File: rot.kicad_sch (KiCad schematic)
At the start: 35 parts, among them J3 52991-0508, J4 M20-7830642, U2 W25Q32JVSSIQ_TR, U3 W25Q32JVSSIQ_TR, U4 W25Q32JVSSIQ_TR, U5 W25Q32JVSSIQ_TR

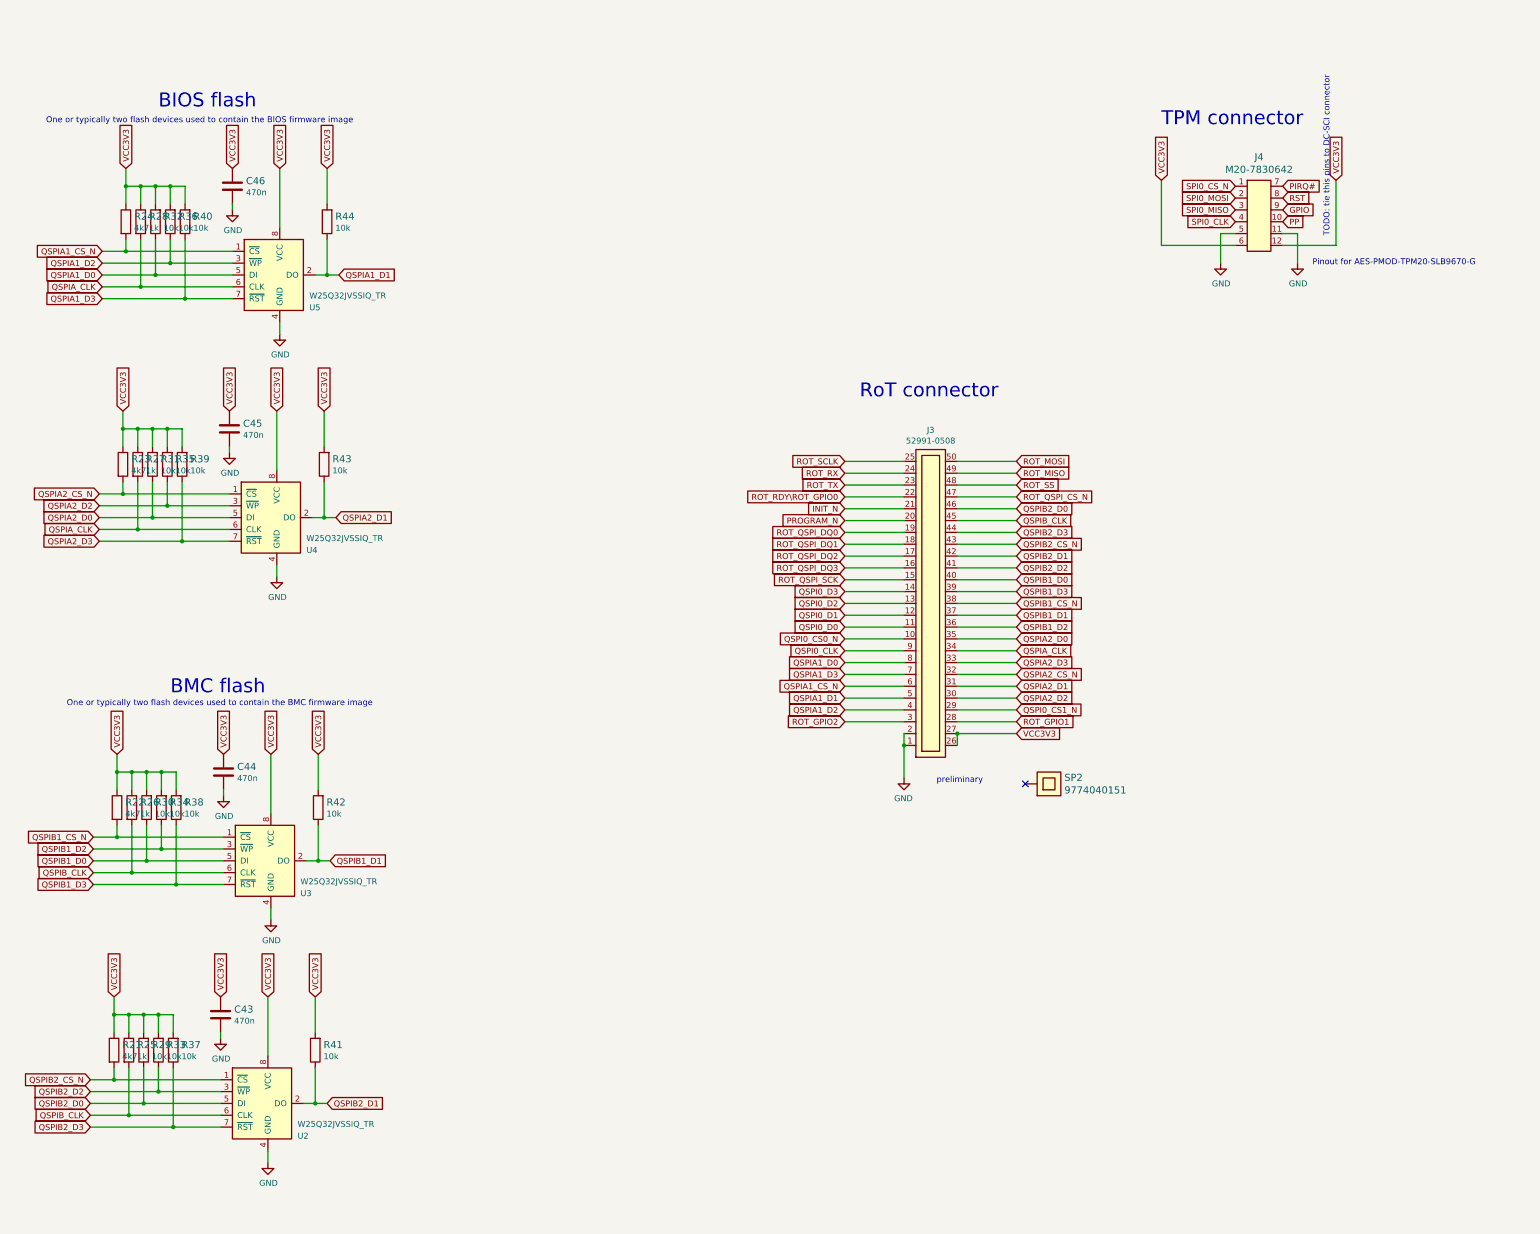
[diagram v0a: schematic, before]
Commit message: [#61392] Convert project to KiCad 7
[#61392] Run globlib

[#61392] Allign components to the grid

[#61392] Update oshw and antmicro logo

[#61392] Standarize ethernet sheet

[#61392] Standarize pcie-conn sheet

[#61392] Standarize rot sheet

[#61392] Standarize edge-connector sheet

[#61392] WIP:Standarize interfaces sheet

[#61392] WIP: Route interfaces sheet

[#61392] Finish standarizing interfaces sheet

[#61392] Update interfaces sheet with fixed 2N7002

[#61392] WIP:Standarize ddr3 sheet

[#61392] Standarize ddr3 sheet

[#61392] Standarize power-supply sheet

[#61392] Standarize fpga power-supply sheet

[#61392] Remove TODO comments from power-banks sheet

[#61392] Standarize fpga-banks sheet

[#61392] Ignore Input pins not driven ERC

[#61392] Clear off grid ERCs

[#61392] Exclude ERC DDR3_VTT_EN NC

[#61392] Bump rev to 1.2.1

[#61392] Bump PCB rev to 1.2.1
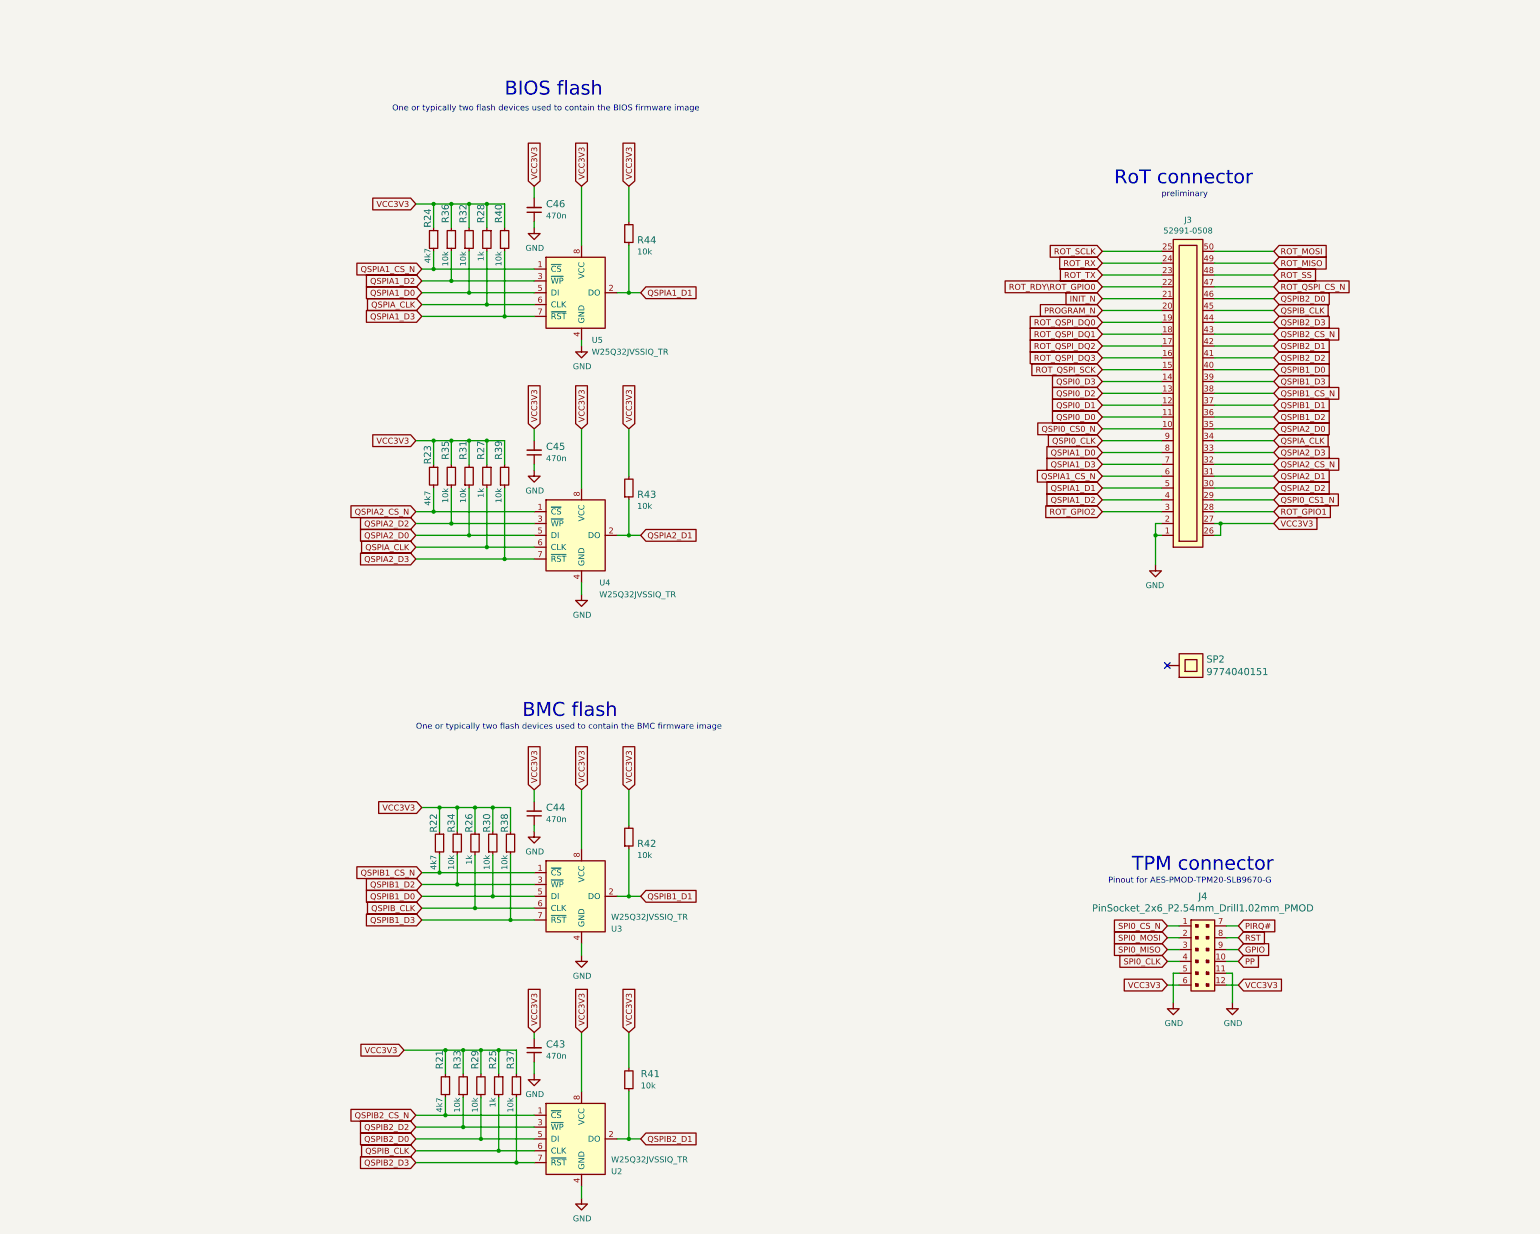
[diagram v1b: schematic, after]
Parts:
- C43, C44, C45, C46: footprint ecp5-dc-scm-footprints:0402-cap -> antmicro-footprints:C_0402_1005Metric; symbol ecp5-dc-scm:C_470n_0402 -> antmicroCapacitors0402:C_470n_0402; Author (none) -> Antmicro; License (none) -> Apache-2.0; Public (none) -> False
- J4: value M20-7830642 -> PinSocket_2x6_P2.54mm_Drill1.02mm_PMOD; footprint ecp5-dc-scm-footprints:PinHeader_6x2_P2.54mm_Vertical_pmod -> antmicro-footprints:PinSocket_2x6_P2.54mm_Drill1.02mm_PMOD; symbol ecp5-dc-scm:M20-7830642 -> antmicroGenericPinSockets:PinSocket_2x6_P2.54mm_Drill1.02mm_PMOD; Author (none) -> Antmicro; License (none) -> Apache-2.0; Manufacturer Molex -> Harwin
- R21, R22, R23, R24: footprint ecp5-dc-scm-footprints:0402-res -> antmicro-footprints:R_0402_1005Metric; symbol ecp5-dc-scm:R_4k7_0402 -> antmicroResistors0402:R_4k7_0402; Author (none) -> Antmicro; License (none) -> Apache-2.0; MPN ERJ2GEJ472X -> CR0402-FX-4701GLF; Manufacturer PANASONIC_ELECTRONIC_COMPONENTS -> Bourns; Public (none) -> False; Tolerance (none) -> 1%
- R25, R26, R27, R28: footprint ecp5-dc-scm-footprints:0402-res -> antmicro-footprints:R_0402_1005Metric; symbol ecp5-dc-scm:R_1k_0402 -> antmicroResistors0402:R_1k_0402; Author (none) -> Antmicro; License (none) -> Apache-2.0; Manufacturer BOURNS -> Bourns; Public (none) -> False; Tolerance (none) -> 1%
- R29, R30, R31, R32, R33, R34, R35, R36, R37, R38, R39, R40, R41, R42, R43, R44: footprint ecp5-dc-scm-footprints:0402-res -> antmicro-footprints:R_0402_1005Metric; symbol ecp5-dc-scm:R_10k_0402 -> antmicroResistors0402:R_10k_0402; Author (none) -> Antmicro; License (none) -> Apache-2.0; MPN CRCW040210K0FKEDHP -> CR0402-FX-1002GLF; Manufacturer VISHAY -> Bourns; Public (none) -> False; Tolerance (none) -> 1%
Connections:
- net GND: now also C43.1, C44.1, C45.1, C46.1; no longer C43.2, C44.2, C45.2, C46.2
- net VCC3V3: now also C43.2, C44.2, C45.2, C46.2; no longer C43.1, C44.1, C45.1, C46.1
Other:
- note removed: "TODO: tie this pins to DC-SCI connector"
- moved on the sheet: C43, C44, C45, C46, J3, R21, R22, R23, R24, R25, R26, R27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

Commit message: [#61392] Import changes to the PCB
[#61392] Fix D2 orientation

[#61392] Fix J2 J1 D6 orientation

[#61392] WIP: PCB Fix caps orienations

[#61392] PCB Fix caps orienations

[#61392] Fix missalligned edge cuts

[#61392] Sync Sch with PCB

[#61392] Fix silk clipped by edge cuts

[#61392] Ignore TP no courtyard drc

[#61392] Update C_0603 footprints

[#61392] Update R_0402 footprints

[#61392] Update Sot-23 footprints

[#61392] Update QFN and IHLP footprints

[#61392] Update remaining footprints

[#61392] Change minimal text height to 0.7mm

[#61392] Clear remaining Silk DRCs

[#61392] Update TPS51200DRCT symbol

[#61392] Update 9774040151

[#61392] Update W25Q32JVS

[#61392] Update ECS-3225MVQ-1000CN-TR

[#61392] Clean ERC

[#61392] Remove obsolete files

[#61392] Synhronize components with library

[#61392] Remove globlib leftovers

[#61392] Synchronize components with libraries (WiP)

[#61392] Clean ERC and DRC

[#61392] Set J5 to DNP

[#61392] Add PCB SHA string, update layer names

[#61392] Update assets

[#62567] Add stackup.csv

[#62567] Input elecric constants for the board stackup

[#62567] Update stackup.csv
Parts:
- removed J3: 52991-0508, ecp5-dc-scm-footprints:529910508, symbol ecp5-dc-scm:52991-0508
- removed SP2: 9774040151, ecp5-dc-scm-footprints:9774040151, symbol ecp5-dc-scm:9774040151
- removed U2, U3, U4, U5: W25Q32JVSSIQ_TR, ecp5-dc-scm-footprints:W25Q32JVSSIQ, symbol ecp5-dc-scm:W25Q32JVSSIQ_TR
- added H2: Spacer_Drill3.7mm_H4mm_9774040151R, antmicro-footprints:Spacer_Drill3.7mm_H4mm_9774040151R, symbol antmicroMechanicalParts:Spacer_Drill3.7mm_H4mm_9774040151R
- added J3: Plug_Molex_SlimStack_2x25_529910508, antmicro-footprints:Conn_Plug_Molex_SlimStack_2x25_529910508, symbol antmicroB2BConnectors:Plug_Molex_SlimStack_2x25_529910508
- added U2, U3, U4, U5: W25Q32JVSSIQ, antmicro-footprints:SOIC-8_5.3x5.3x2mm_P1.27mm, symbol antmicroMemory:W25Q32JVSSIQ
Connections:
- net GND: now also J3.2, J3.4, U2.4 (VSS), U3.4 (VSS), U4.4 (VSS), U5.4 (VSS)
- net INIT_N: now also J3.42
- net PROGRAM_N: now also J3.40
- net QSPI0_CLK: now also J3.18
- net QSPI0_CS0_N: now also J3.20
- net QSPI0_CS1_N: now also J3.7
- net QSPI0_D0: now also J3.22
- net QSPI0_D1: now also J3.24
- net QSPI0_D2: now also J3.26
- net QSPI0_D3: now also J3.28
- net QSPIA1_CS_N: now also J3.12, U5.1 (~{CS})
- net QSPIA1_D0: now also J3.16, U5.5 (SI/IO0)
- net QSPIA1_D1: now also J3.10, U5.2 (SO/IO1)
- net QSPIA1_D2: now also J3.8, U5.3 (~{WP}/IO2)
- net QSPIA1_D3: now also J3.14, U5.7 (~{HOLD}/IO3)
- net QSPIA2_CS_N: now also J3.13, U4.1 (~{CS})
- net QSPIA2_D0: now also J3.19, U4.5 (SI/IO0)
- net QSPIA2_D1: now also J3.11, U4.2 (SO/IO1)
- net QSPIA2_D2: now also J3.9, U4.3 (~{WP}/IO2)
- net QSPIA2_D3: now also J3.15, U4.7 (~{HOLD}/IO3)
- net QSPIA_CLK: now also J3.17, U4.6 (SCLK), U5.6 (SCLK)
- net QSPIB1_CS_N: now also J3.25, U3.1 (~{CS})
- net QSPIB1_D0: now also J3.29, U3.5 (SI/IO0)
- net QSPIB1_D1: now also J3.23, U3.2 (SO/IO1)
- net QSPIB1_D2: now also J3.21, U3.3 (~{WP}/IO2)
- net QSPIB1_D3: now also J3.27, U3.7 (~{HOLD}/IO3)
- net QSPIB2_CS_N: now also J3.35, U2.1 (~{CS})
- net QSPIB2_D0: now also J3.41, U2.5 (SI/IO0)
- net QSPIB2_D1: now also J3.33, U2.2 (SO/IO1)
- net QSPIB2_D2: now also J3.31, U2.3 (~{WP}/IO2)
- net QSPIB2_D3: now also J3.37, U2.7 (~{HOLD}/IO3)
- net QSPIB_CLK: now also J3.39, U2.6 (SCLK), U3.6 (SCLK)
- net ROT_GPIO1: now also J3.5
- net ROT_GPIO2: now also J3.6
- net ROT_MISO: now also J3.47
- net ROT_MOSI: now also J3.49
- net ROT_QSPI_CS_N: now also J3.43
- net ROT_QSPI_DQ0: now also J3.38
- net ROT_QSPI_DQ1: now also J3.36
- net ROT_QSPI_DQ2: now also J3.34
- net ROT_QSPI_DQ3: now also J3.32
- net ROT_QSPI_SCK: now also J3.30
- net ROT_RDY\ROT_GPIO0: now also J3.44
- net ROT_RX: now also J3.48
- net ROT_SCLK: now also J3.50
- net ROT_SS: now also J3.45
- net ROT_TX: now also J3.46
- net VCC3V3: now also J3.1, J3.3, U2.8 (VCC), U3.8 (VCC), U4.8 (VCC), U5.8 (VCC)
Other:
- moved on the sheet: C43, C44, C45, C46, R21, R22, R23, R24, R25, R26, R27, R28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
